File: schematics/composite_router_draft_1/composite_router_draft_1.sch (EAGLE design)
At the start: 44 parts, among them U1 ARDUINO-MEGA

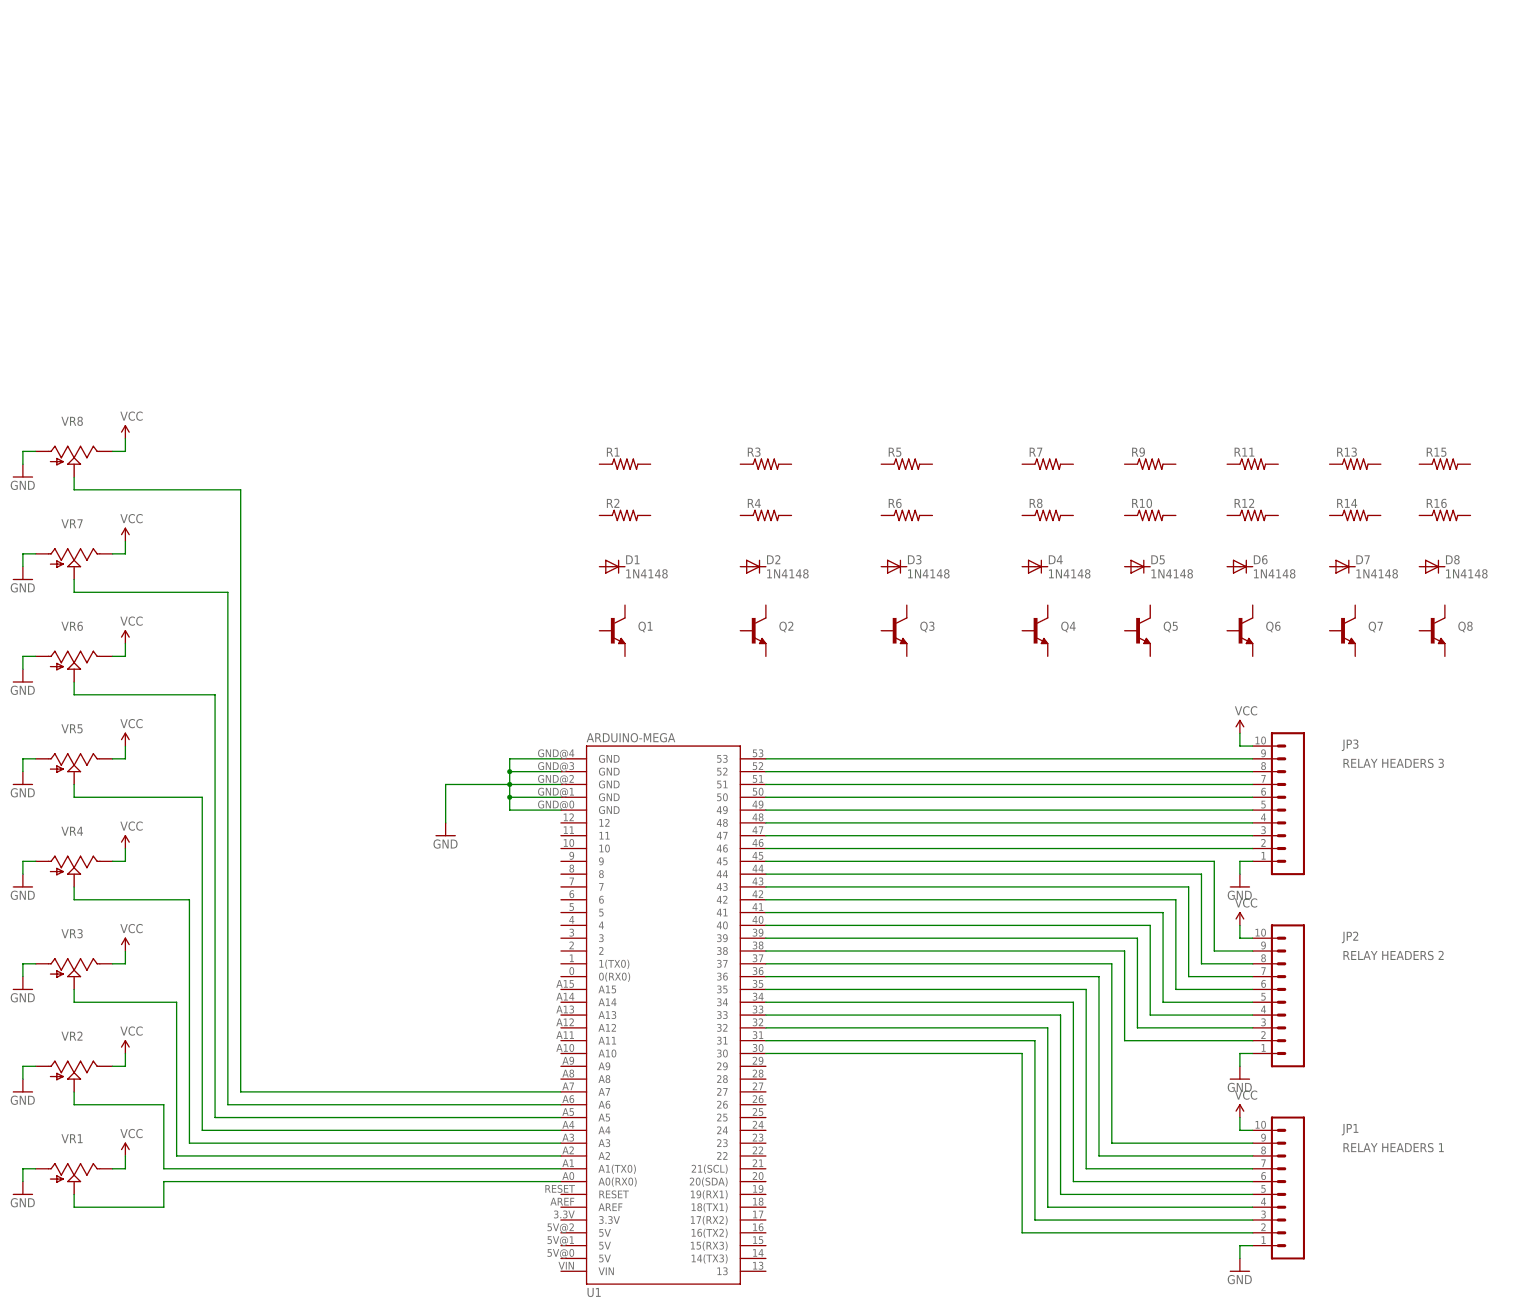
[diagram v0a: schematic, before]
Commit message: tested arduino relay
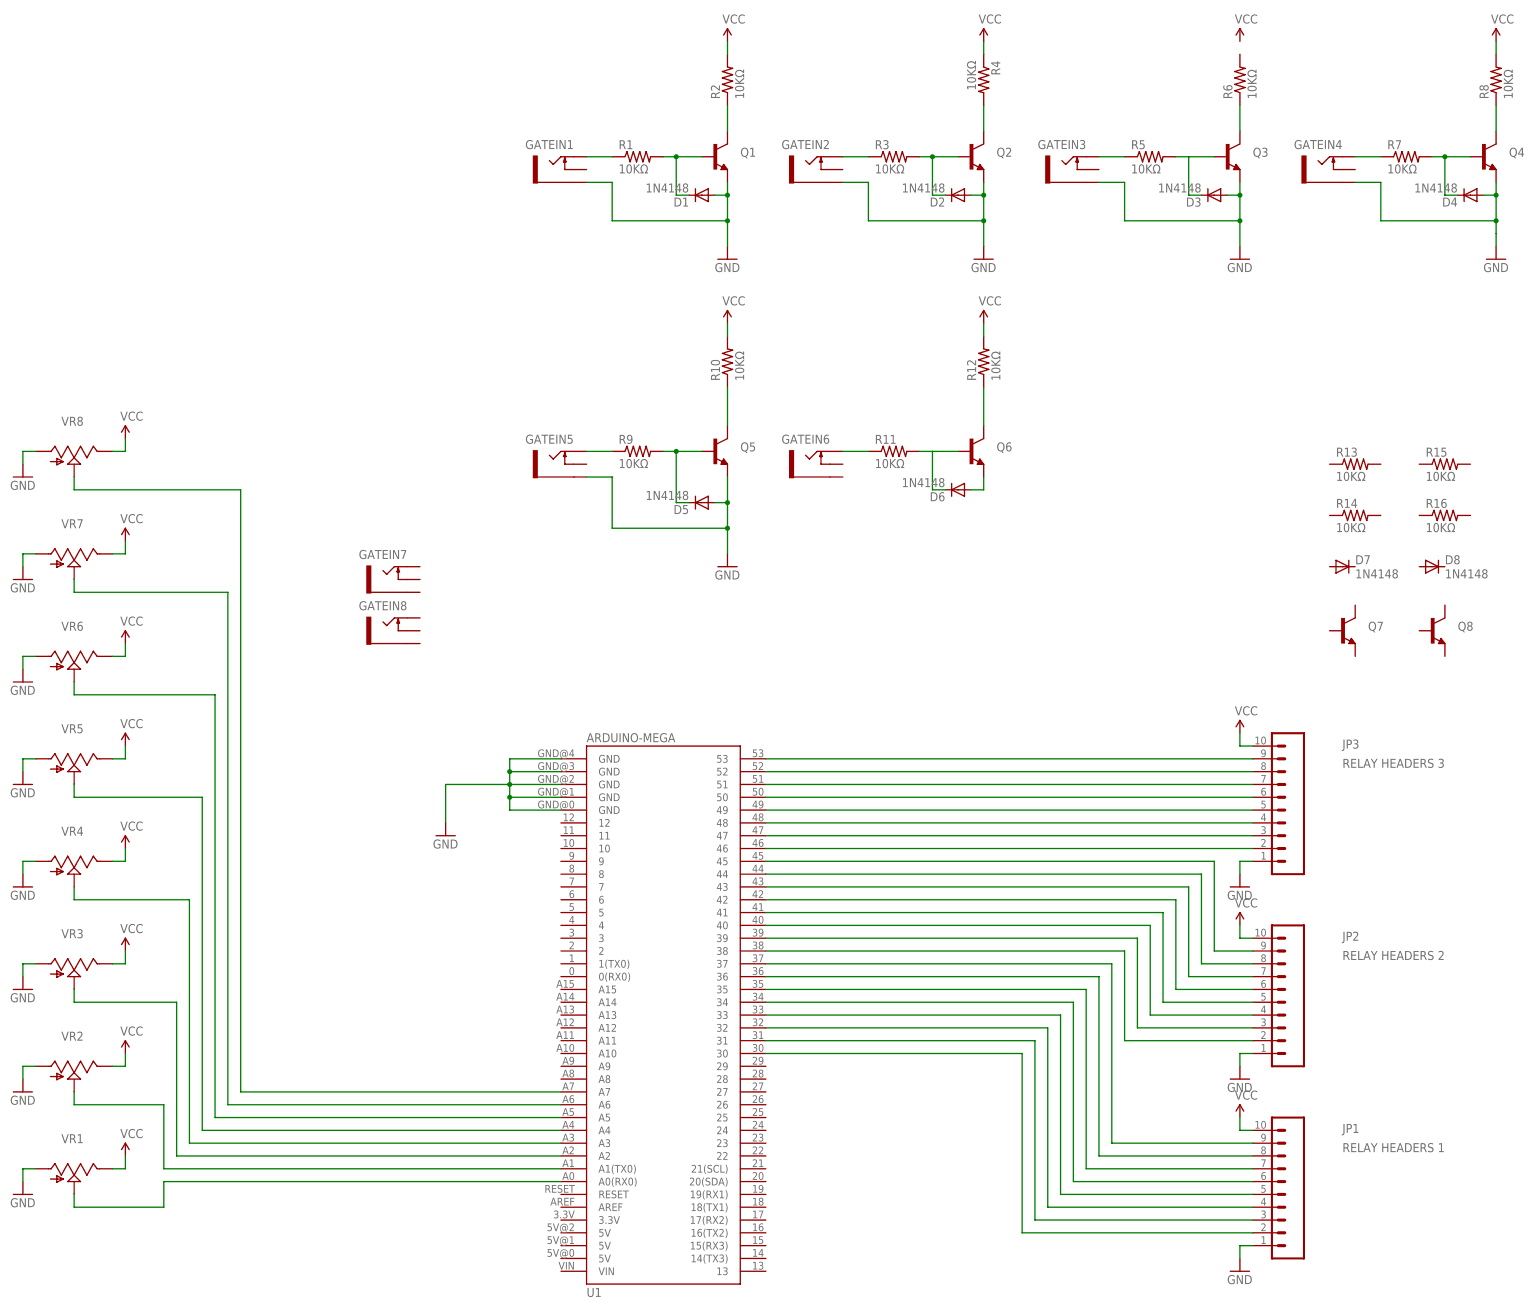
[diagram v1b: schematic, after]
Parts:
- added GATEIN1, GATEIN2, GATEIN3, GATEIN4, GATEIN5, GATEIN6, GATEIN7, GATEIN8: THONKICONNNEW, MusicThingModular:THONKICONNNEW
- R1, R10, R11, R12, R13, R14, R15, R16, R2, R3, R4, R5, R6, R7, R8, R9: value (none) -> 10KΩ
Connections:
- new net N$25: GATEIN1.TIP, R1.1
- new net N$34: D1.C, Q1.B, R1.2
- new net N$35: GATEIN3.TIP, R5.1
- new net N$36: D3.C, Q3.B, R5.2
- new net N$37: Q1.C, R2.1
- new net N$38: D2.C, Q2.B, R3.2
- new net N$39: Q2.C, R4.2
- new net N$40: GATEIN2.TIP, R3.1
- new net N$41: Q3.C, R6.1
- new net N$44: GATEIN4.TIP, R7.1
- new net N$45: D4.C, Q4.B, R7.2
- new net N$46: Q4.C, R8.1
- new net N$48: GATEIN5.TIP, R9.1
- new net N$49: D5.C, Q5.B, R9.2
- new net N$50: Q5.C, R10.1
- new net N$53: GATEIN6.TIP, R11.1
- new net N$54: D6.C, Q6.B, R11.2
- new net N$55: Q6.C, R12.1
- new net N$56: D6.A, Q6.E
- net GND: now also D1.A, D2.A, D3.A, D4.A, D5.A, GATEIN1.SLEEVE, GATEIN2.SLEEVE, GATEIN3.SLEEVE, GATEIN4.SLEEVE, GATEIN5.SLEEVE, Q1.E, Q2.E, Q3.E, Q4.E, Q5.E
- net VCC: now also R10.2, R12.2, R2.2, R4.1, R8.2
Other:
- moved on the sheet: D1, D2, D3, D4, D5, D6, Q1, Q2, Q3, Q4, Q5, Q6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
